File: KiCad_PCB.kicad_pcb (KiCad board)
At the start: 2 copper layers, 84.9 x 38.1 mm, 24 parts, among them SW1 SW_Push, U1 ATmega32U4-AU, Y1 Crystal_GND24_Small

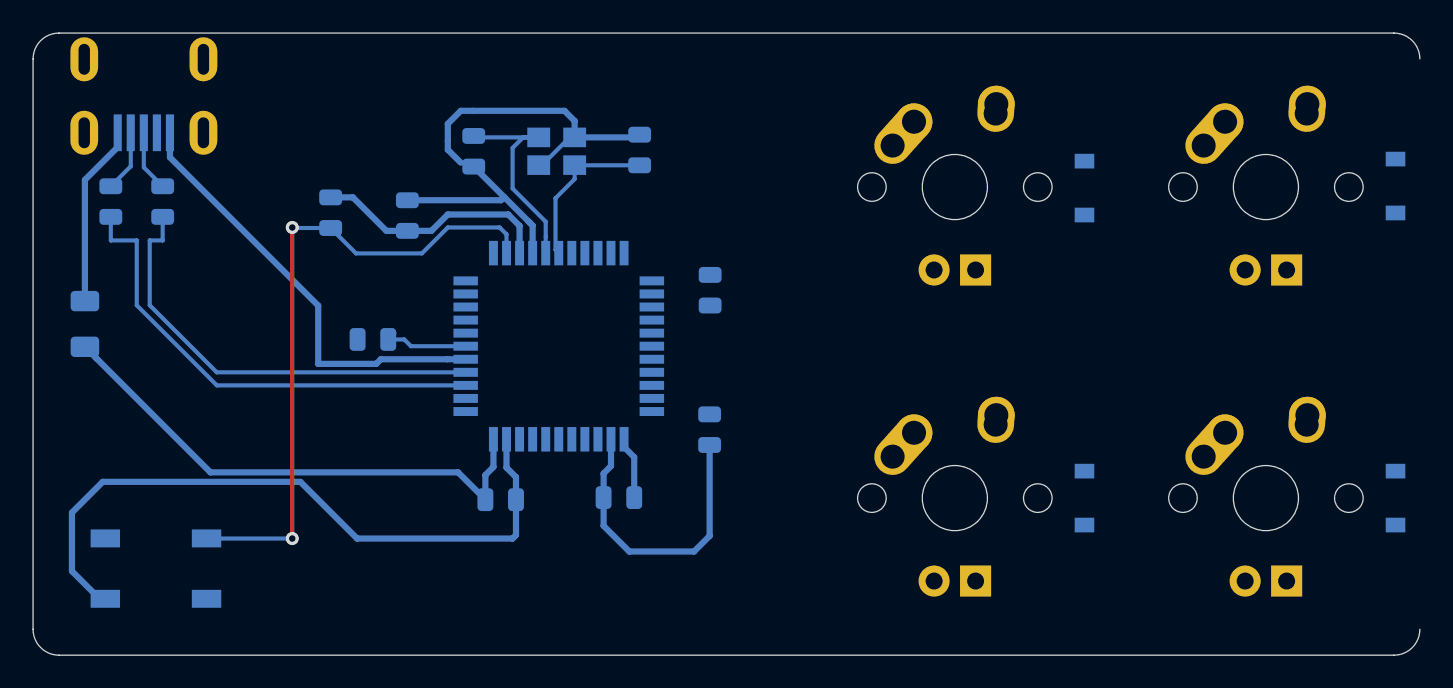
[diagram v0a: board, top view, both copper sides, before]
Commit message: Finished PCB
The keyboard pcb tutorial from: https://wiki.ai03.com/books/pcb-design/chapter/pcb-designer-guide is complete.
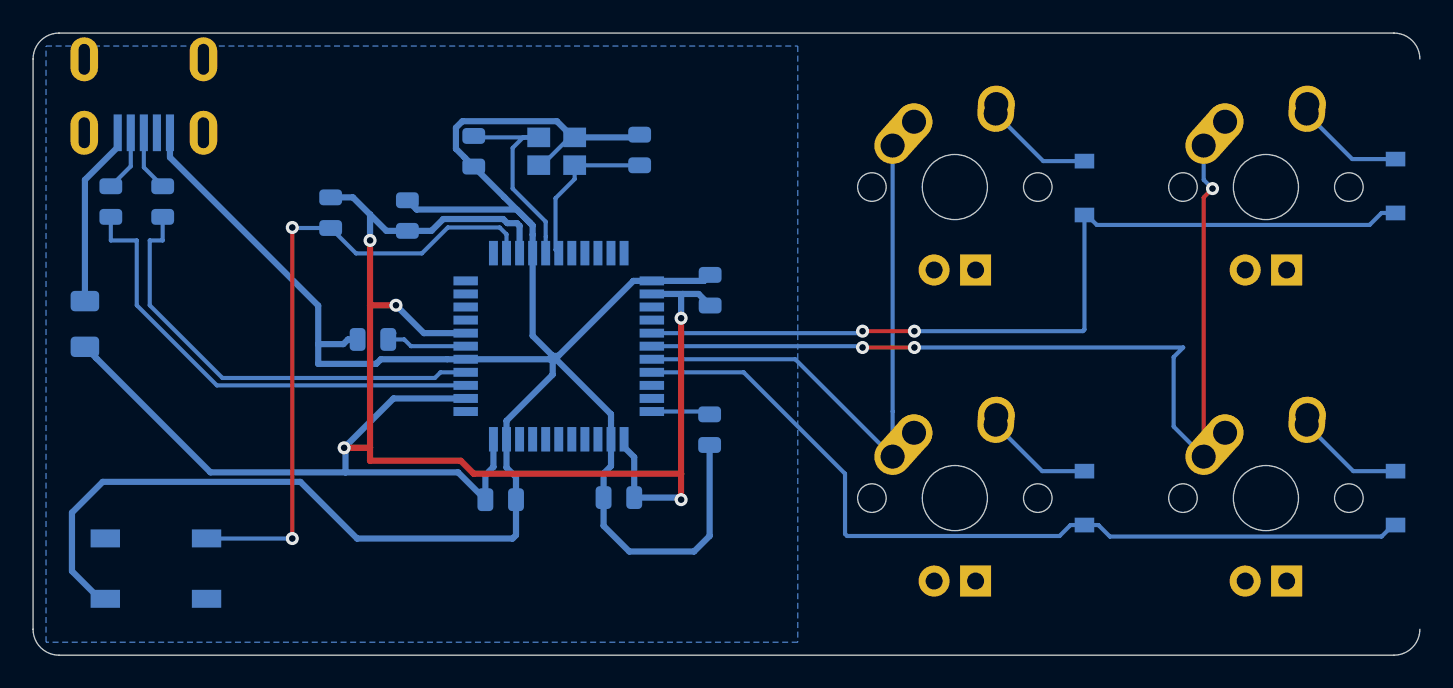
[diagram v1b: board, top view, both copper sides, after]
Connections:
- U1 pad 27: Net-(U1-Pad27) -> Row0
- U1 pad 28: Net-(U1-Pad28) -> Col1
- U1 pad 29: Net-(U1-Pad29) -> Col0
- U1 pad 30: Net-(U1-Pad30) -> Row1
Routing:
- net +5V: track 50.9 -> 123.0 mm, vias 0 -> 5
- net Col1: track 0.00 -> 59.8 mm, vias 0 -> 3
- net Row0: track 0.00 -> 53.2 mm, vias 0 -> 2
- net Row1: track 0.00 -> 52.7 mm
- net GND: track 119.6 -> 159.8 mm
- net Col0: track 0.00 -> 36.3 mm
- net Net-(D1-Pad2): track 0.00 -> 6.64 mm
- net Net-(D4-Pad2): track 0.00 -> 6.62 mm
- net Net-(D3-Pad2): track 0.00 -> 6.62 mm
- net Net-(D2-Pad2): track 0.00 -> 6.59 mm
- net Net-(R4-Pad2): track 0.00 -> 3.61 mm
- added copper zone on B.Cu, net GND
